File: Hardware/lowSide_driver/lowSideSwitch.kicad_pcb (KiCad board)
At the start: 2 copper layers, 140 x 40 mm, 36 parts, among them J1 LEDS_0-15, J2 Conn_01x16, J3 Conn_01x16, J4 Conn_01x16, J5 Conn_01x10, J6 Conn_01x10, J7 Conn_01x02, U1 TLC591, U2 TLC591, U3 TLC591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

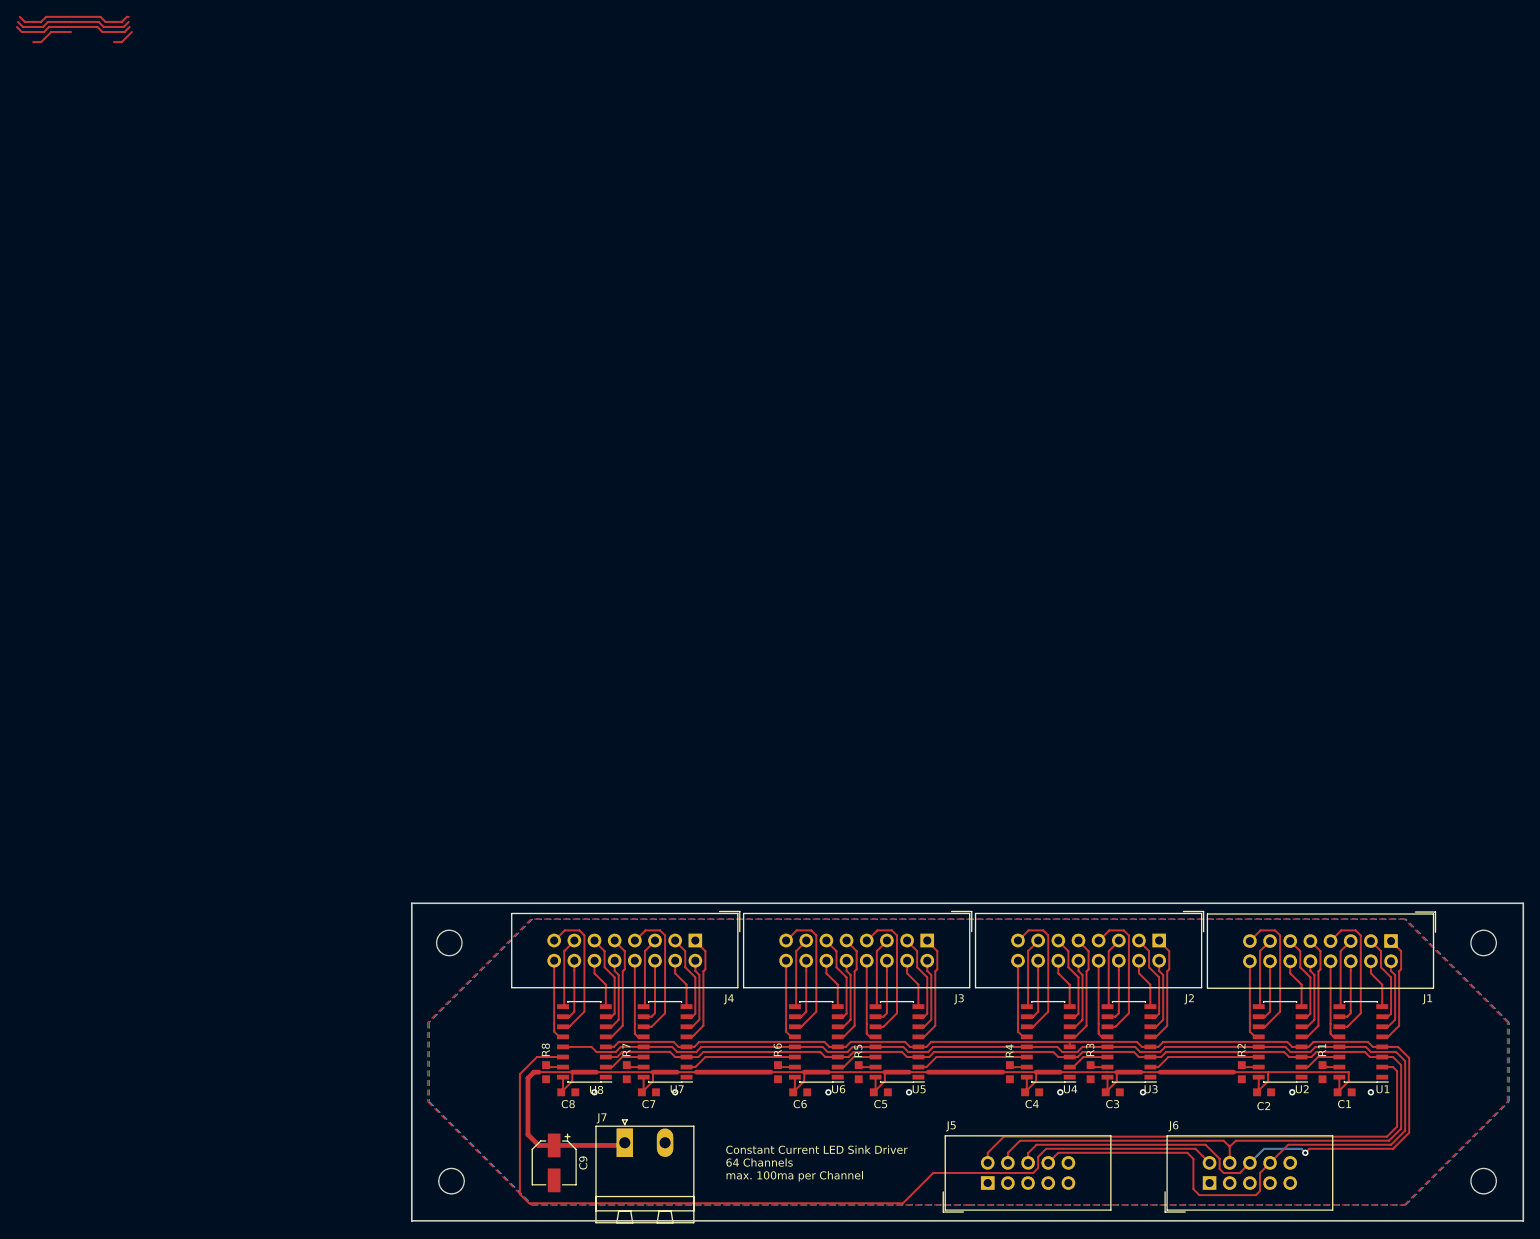
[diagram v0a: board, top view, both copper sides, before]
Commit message: Software: Added timer for LE and OE
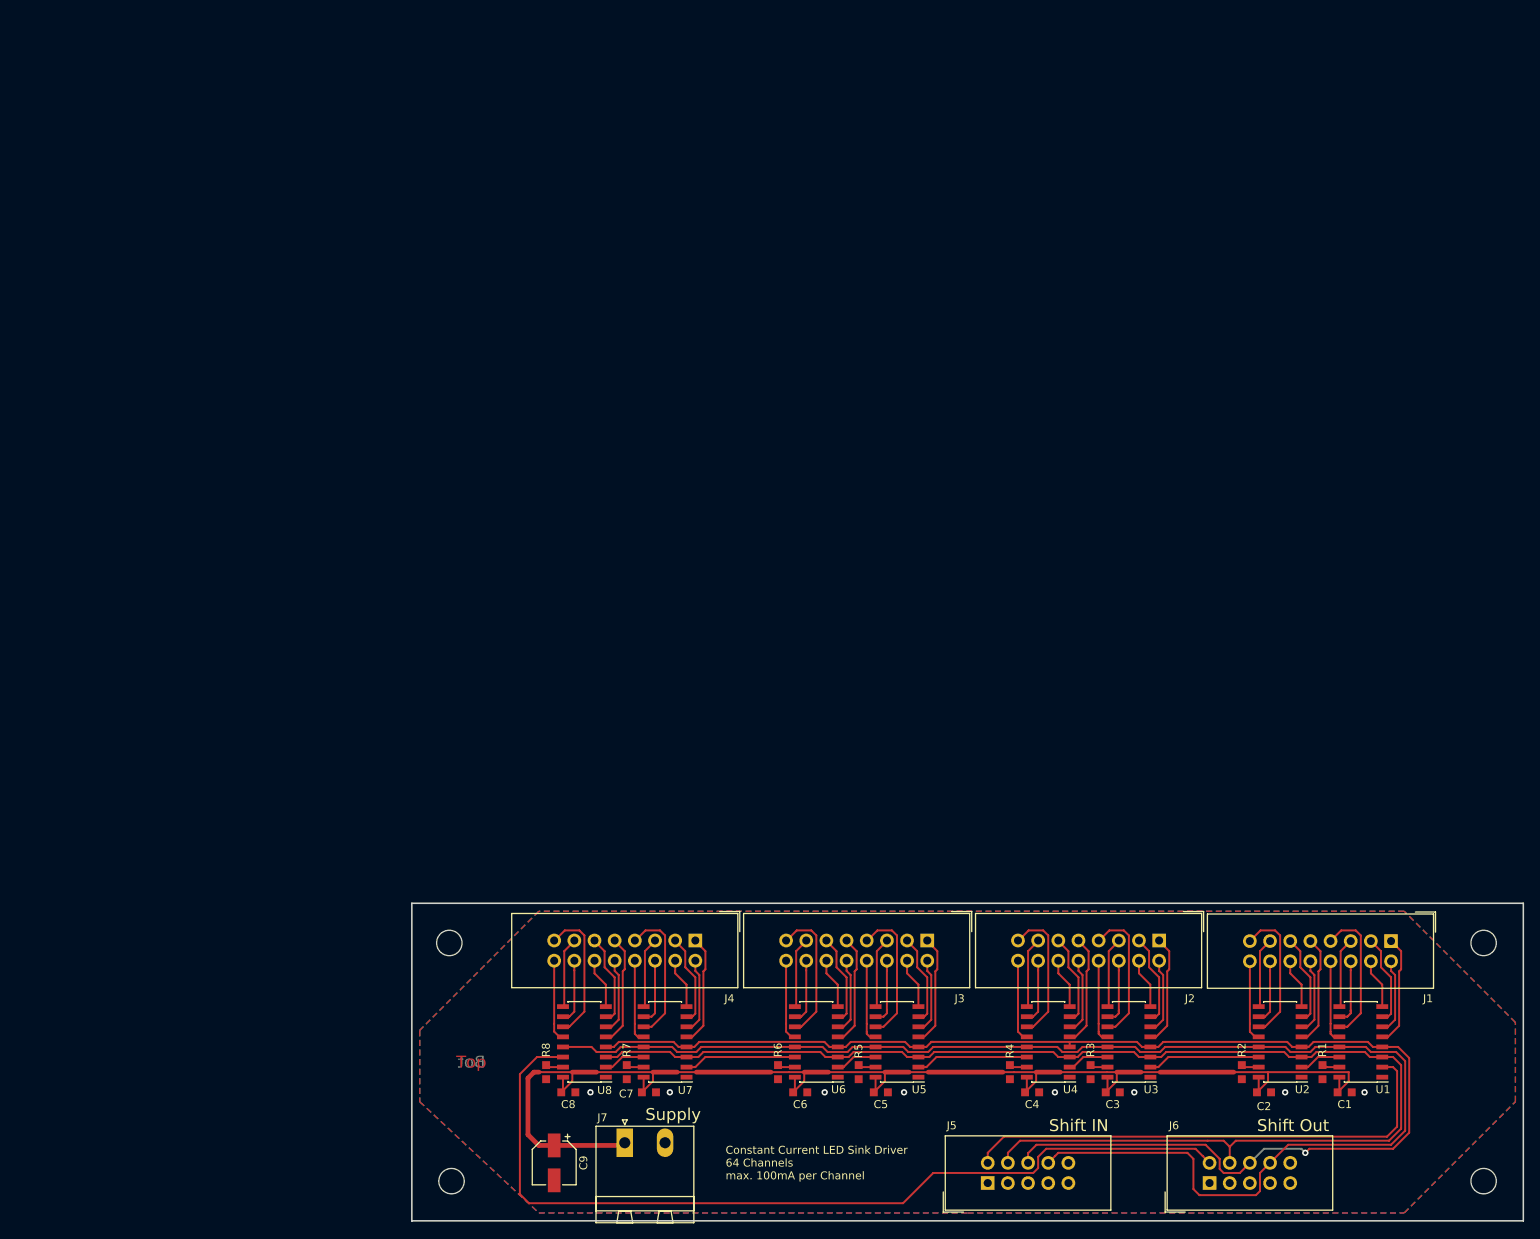
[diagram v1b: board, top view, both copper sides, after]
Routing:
- net (no net): track 53.1 -> 0.00 mm
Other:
- board text added: "Bot"
- board text added: "Constant Current LED Sink Driver 64 Channels max. 100mA per Channel"
- board text added: "Shift IN"
- board text added: "Shift Out"
- board text added: "Supply"
- board text added: "Top"
- board text removed: "Constant Current LED Sink Driver 64 Channels max. 100ma per Channel"
